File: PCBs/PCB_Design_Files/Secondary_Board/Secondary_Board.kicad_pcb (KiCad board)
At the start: 2 copper layers, 0 parts

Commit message: Bandgap/Ptat layout on secondary board. Updated grounded mounting holes on schematic, fix all DRC warnings
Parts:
- added C1: .1u, Project Footprints:0603_capacitor, F.Cu at (132.1, 94.5)
- added H1: MountingHole_Pad, MountingHole:MountingHole_2.2mm_M2_DIN965_Pad, F.Cu at (144.7, 70.4)
- added H2: MountingHole_Pad, MountingHole:MountingHole_2.2mm_M2_DIN965_Pad, F.Cu at (111.4, 70.4)
- added H3: MountingHole_Pad, MountingHole:MountingHole_2.2mm_M2_DIN965_Pad, F.Cu at (145.0, 120.0)
- added H4: MountingHole_Pad, MountingHole:MountingHole_2.2mm_M2_DIN965_Pad, F.Cu at (111.0, 120.0)
- added IC1: TLV2333IDGKR, Project Footprints:TLV2333IDGKR, F.Cu at (127.8, 94.7)
- added Q1: DMMT3904W-7-F, Project Footprints:DMMT3904W_Dual_NPN, F.Cu at (127.7, 88.8)
- added Q2: DMMT3904W-7-F, Project Footprints:DMMT3904W_Dual_NPN, F.Cu at (127.7, 85.8)
- added R3: 40k, Project Footprints:0603_resistor, F.Cu at (135.1, 94.4)
- added R4: 2.5k, Project Footprints:0603_resistor, F.Cu at (119.0, 87.2)
- added R5: 5k, Project Footprints:0603_resistor, F.Cu at (119.0, 91.0)
- added R6: 1k, Project Footprints:0603_resistor, F.Cu at (119.0, 83.4)
- added R7: 1k, Project Footprints:0603_resistor, F.Cu at (122.4, 82.5)
- added R8: 103, Project Footprints:0603_resistor, F.Cu at (132.6, 85.9)
- added R9: 2040, Project Footprints:0603_resistor, F.Cu at (127.5, 91.6)
- added U1: DMMT5401-7-F, Project Footprints:DMMT5401_Dual_PNP, F.Cu at (133.8, 90.3)
- added U2: DMMT5401-7-F, Project Footprints:DMMT5401_Dual_PNP, F.Cu at (121.7, 94.7)
- added U3: DMMT5401-7-F, Project Footprints:DMMT5401_Dual_PNP, F.Cu at (122.7, 90.0)
- added U4: DMMT5401-7-F, Project Footprints:DMMT5401_Dual_PNP, F.Cu at (122.6, 85.9)
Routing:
- net Net-(IC1-OUT_B): track 0.00 -> 32.6 mm, vias 0 -> 2
- net Net-(IC1-+IN_B): track 0.00 -> 31.5 mm
- net Net-(IC1--IN_A): track 0.00 -> 21.7 mm
- net Net-(IC1-+IN_A): track 0.00 -> 13.6 mm, vias 0 -> 2
- net GND: track 0.00 -> 13.1 mm, vias 0 -> 7
- net Net-(IC1-OUT_A): track 0.00 -> 11.4 mm
- net Net-(Q1-B2): track 0.00 -> 11.0 mm
- net /PTAT_Bandgap/V_bandgap: track 0.00 -> 10.7 mm
- net +3V3: track 0.00 -> 6.36 mm, vias 0 -> 5
- net Net-(U1-B1): track 0.00 -> 5.67 mm
- net Net-(U4-E1): track 0.00 -> 5.26 mm
- net Net-(U4-E2): track 0.00 -> 4.80 mm
- net /PTAT_Bandgap/V_ptat: track 0.00 -> 2.78 mm
- added copper zone on In2.Cu, net (none)
- added copper zone on F.Cu, net +3V3
- added copper zone on In2.Cu, net +3V3
- added copper zone on In1.Cu, net GND
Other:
- board outline added: 40.3 x 57.1 mm
- copper layers 2 -> 4
- rule pad_to_mask_clearance: 1 -> 0
- board text added: "CONTACT BELOW"

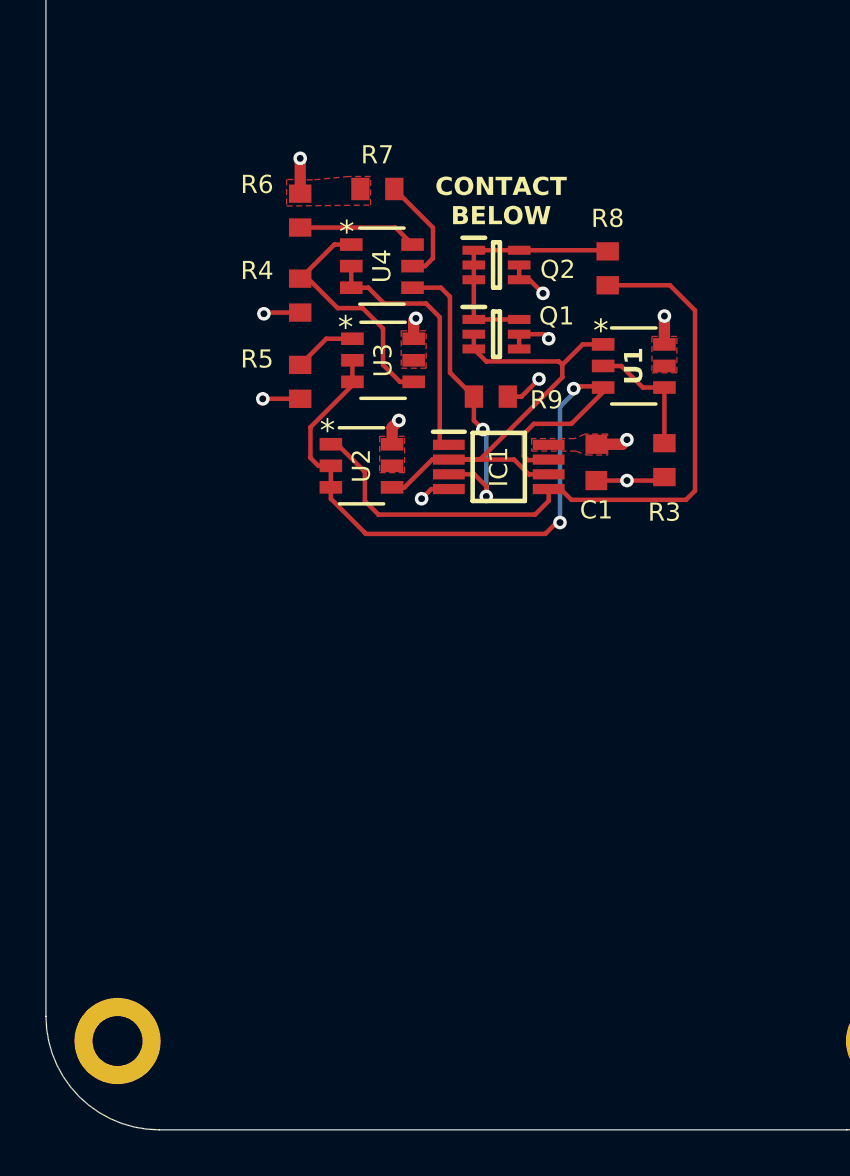
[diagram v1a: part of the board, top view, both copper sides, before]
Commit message: Added header and ffc connector to both boards + update libraries. Updated BOM
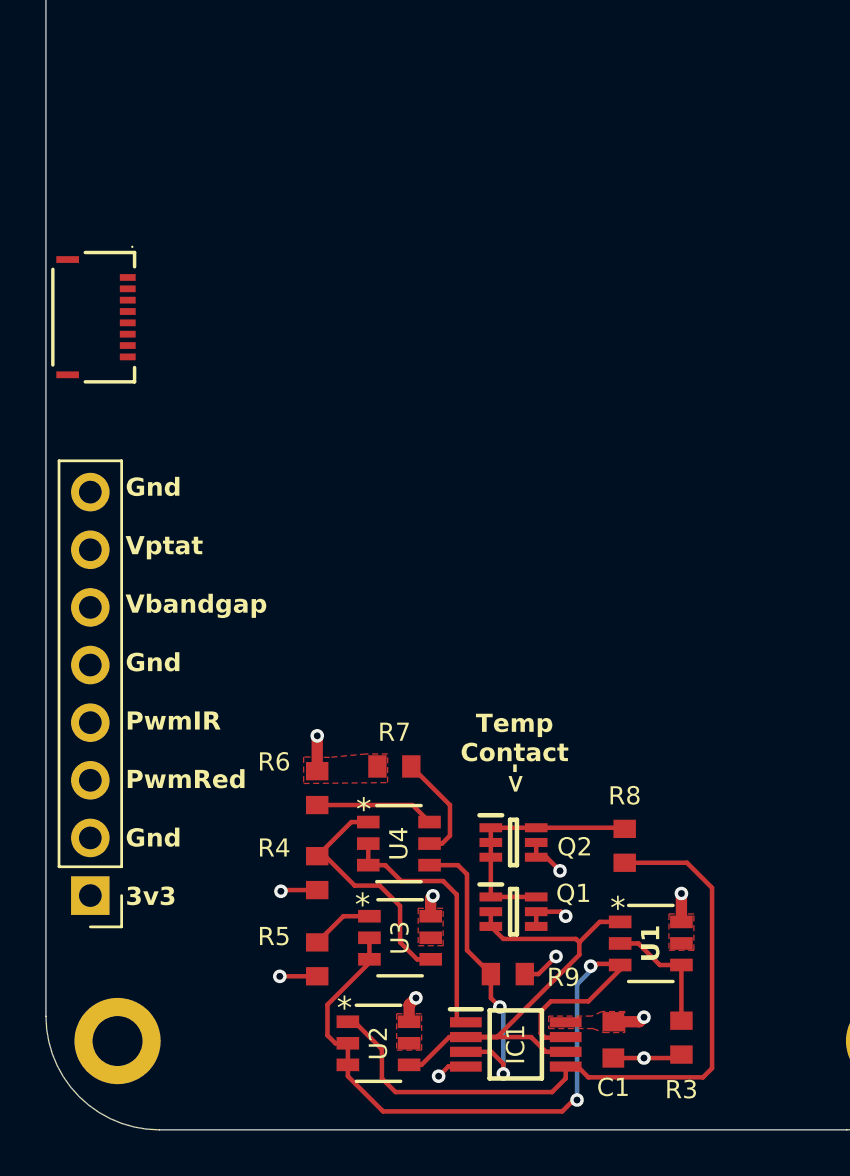
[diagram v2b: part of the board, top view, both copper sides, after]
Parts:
- added J1: Conn_FFC_8pin, Project Footprints:Conn_FFC_8pin, F.Cu at (110.0, 88.1)
- added J2: Conn_01x08_Pin, Connector_PinHeader_2.54mm:PinHeader_1x08_P2.54mm_Vertical, F.Cu at (109.8, 113.6)
- moved C1 25.5 mm to (132.8, 120.0)
- moved IC1 25.5 mm to (128.6, 120.2)
- moved R4 25.5 mm to (119.8, 112.6)
- moved R5 25.5 mm to (119.8, 116.4)
- moved R7 25.5 mm to (123.2, 107.9)
- moved R8 25.5 mm to (133.3, 111.4)
- moved U1 25.5 mm to (134.5, 115.7)
- moved U2 25.5 mm to (122.5, 120.1)
- moved U3 25.5 mm to (123.5, 115.5)
- moved Q1 25.5 mm to (128.4, 114.3)
- moved Q2 25.5 mm to (128.4, 111.2)
- moved R9 25.5 mm to (128.2, 117.0)
- moved R3 25.5 mm to (135.8, 119.8)
- moved R6 25.5 mm to (119.8, 108.9)
- moved U4 25.5 mm to (123.4, 111.3)
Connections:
- net /PTAT_Bandgap/V_bandgap renamed /V_bandgap
- net /PTAT_Bandgap/V_ptat renamed /V_ptat
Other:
- board text added: "->"
- board text added: "Gnd Vptat Vbandgap Gnd PwmIR PwmRed Gnd 3v3"
- board text added: "Temp Contact"
- board text removed: "CONTACT BELOW"

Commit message: update
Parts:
- added BT1: Battery, Connector_JST:JST_PH_S2B-PH-K_1x02_P2.00mm_Horizontal, F.Cu at (120.5, 86.0)
- added C2: 4.7u, Capacitor_SMD:C_0603_1608Metric, F.Cu at (120.5, 80.0)
- added C3: 4.7u, Capacitor_SMD:C_0603_1608Metric, F.Cu at (120.5, 81.5)
- added C4: 4.7u, Capacitor_SMD:C_0603_1608Metric, F.Cu at (86.0, 71.5)
- added C5: 4.7u, Capacitor_SMD:C_0603_1608Metric, F.Cu at (86.0, 74.0)
- added C6: 4.7u, Capacitor_SMD:C_0603_1608Metric, F.Cu at (86.0, 76.5)
- added C7: 4.7u, Capacitor_SMD:C_0603_1608Metric, F.Cu at (86.0, 79.0)
- added D1: 15N122B, Diode_THT:D_DO-35_SOD27_P7.62mm_Horizontal, F.Cu at (89.6, 67.0)
- added L1: CIGT201610LH1R0MNE, Project Footprints:RES_CIGT201610_SAM, F.Cu at (90.3, 80.2)
- added Q3: MMBT3904, Project Footprints:SOT23_FAS, F.Cu at (91.5, 71.2)
- added Q4: MMBT3904, Project Footprints:SOT23_FAS, F.Cu at (91.5, 76.1)
- added R1: 73.2k, Project Footprints:0603_resistor, F.Cu at (81.7, 66.8)
- added R10: 250, Project Footprints:0603_resistor, F.Cu at (81.7, 73.1)
- added R11: 100, Project Footprints:0603_resistor, F.Cu at (81.7, 76.3)
- added R12: 3.96k, Project Footprints:0603_resistor, F.Cu at (81.7, 79.4)
- added R13: 10k, Project Footprints:0603_resistor, F.Cu at (81.7, 82.6)
- added R2: 10k, Project Footprints:0603_resistor, F.Cu at (81.7, 69.9)
- added U5: TPS61023DRLR, Project Footprints:DRL0006A, F.Cu at (123.5, 79.5)
- added U6: TLV9101IDCKR, Project Footprints:SC70-5_DCK_TEX, F.Cu at (96.1, 80.6)
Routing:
- net +3.7V: track 0.00 -> 1.72 mm
- net Net-(U5-SW): track 0.00 -> 1.62 mm

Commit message: updated bg_ptat
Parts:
- added C8: .1u, Project Footprints:0603_capacitor, F.Cu at (116.2, 111.4)
- added U7: TLV9002, Project Footprints:TLV9002, F.Cu at (116.5, 114.6)
- R4: value 2.5k -> 2.2k
- R8: value 103 -> 105
- R9: value 2040 -> 2050
- moved C1 1.41 mm to (134.2, 120.1)
- moved Q1 1.41 mm to (129.8, 114.5)
- moved Q2 1.41 mm to (129.8, 111.4)
- moved R3 1.41 mm to (137.2, 120.0)
- moved R8 1.41 mm to (134.7, 111.5)
- moved R9 1.41 mm to (129.6, 117.2)
- moved U1 1.41 mm to (135.9, 115.9)
- moved U4 1.41 mm to (124.8, 111.5)
- moved R5 1.41 mm to (121.2, 116.6)
- moved R6 1.41 mm to (121.2, 109.0)
- moved R7 1.41 mm to (124.6, 108.1)
- moved U3 1.41 mm to (124.8, 115.6)
- moved R4 1.41 mm to (121.2, 112.8)
- moved U2 1.41 mm to (123.9, 120.3)
- moved IC1 1.41 mm to (129.9, 120.3)
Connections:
- J1 pad 2: GND -> +5V
- J1 pad 6: /V_bandgap -> /V_ptat
- J1 pad 7: /V_ptat -> /V_bandgap
- J2 pad 2: GND -> +5V
- J2 pad 6: /V_bandgap -> /V_ptat
- J2 pad 7: /V_ptat -> /V_bandgap
- R4 pad 1: /V_bandgap -> /PTAT_Bandgap/Vbg
- R5 pad 1: /V_ptat -> /PTAT_Bandgap/Vptat
- U3 pad 1: /V_ptat -> /PTAT_Bandgap/Vptat
- U3 pad 4: /V_bandgap -> /PTAT_Bandgap/Vbg
- U4 pad 1: /V_bandgap -> /PTAT_Bandgap/Vbg
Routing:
- net /V_ptat: track 2.78 -> 19.2 mm
- net /PTAT_Bandgap/Vbg: track 0.00 -> 15.4 mm
- net /V_bandgap: track 10.7 -> 21.4 mm
- net /PTAT_Bandgap/Vptat: track 0.00 -> 8.37 mm
- net GND: track 13.1 -> 16.0 mm, vias 7 -> 9
- net +3V3: track 6.36 -> 8.06 mm, vias 5 -> 6
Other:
- board text added: "Gnd Vbandgap Vptat Gnd PwmIR PwmRed Gnd 3v3"
- board text removed: "Gnd Vptat Vbandgap Gnd PwmIR PwmRed Gnd 3v3"

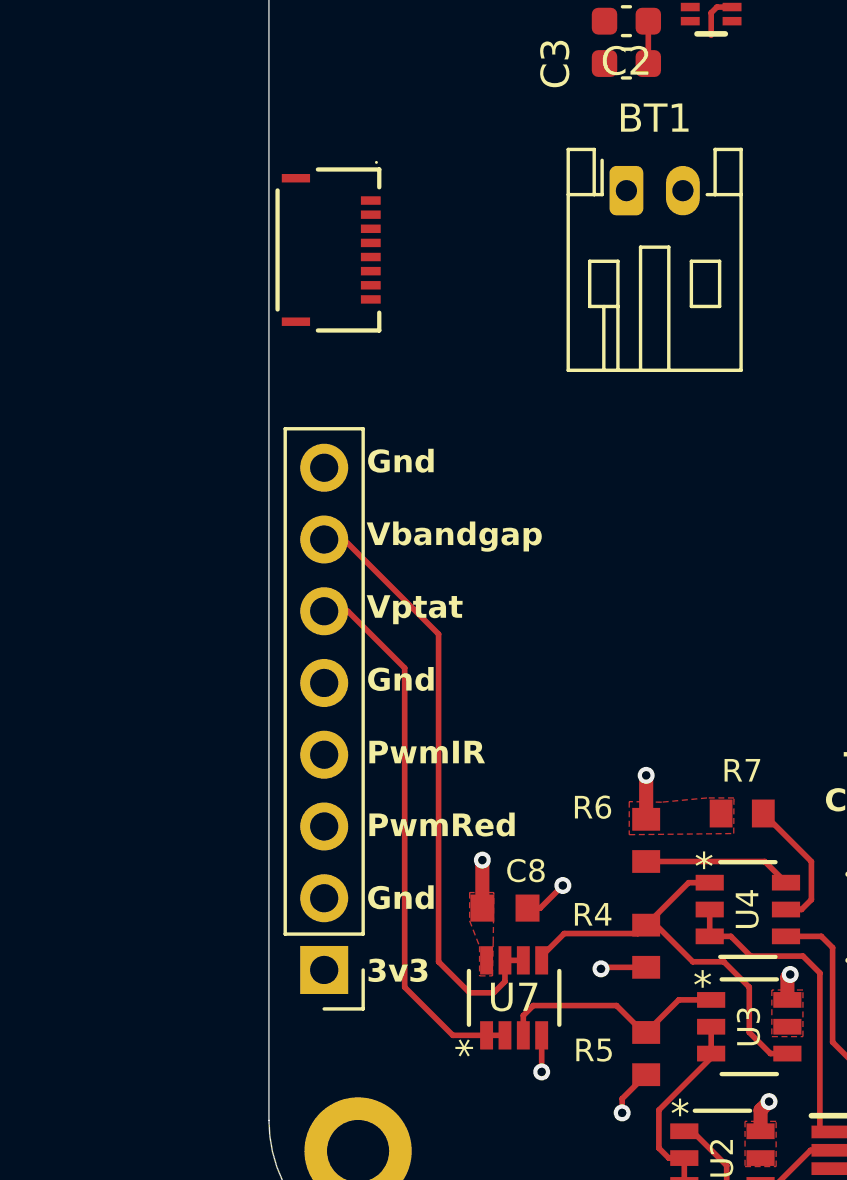
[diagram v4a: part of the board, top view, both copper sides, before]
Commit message: connected connectors
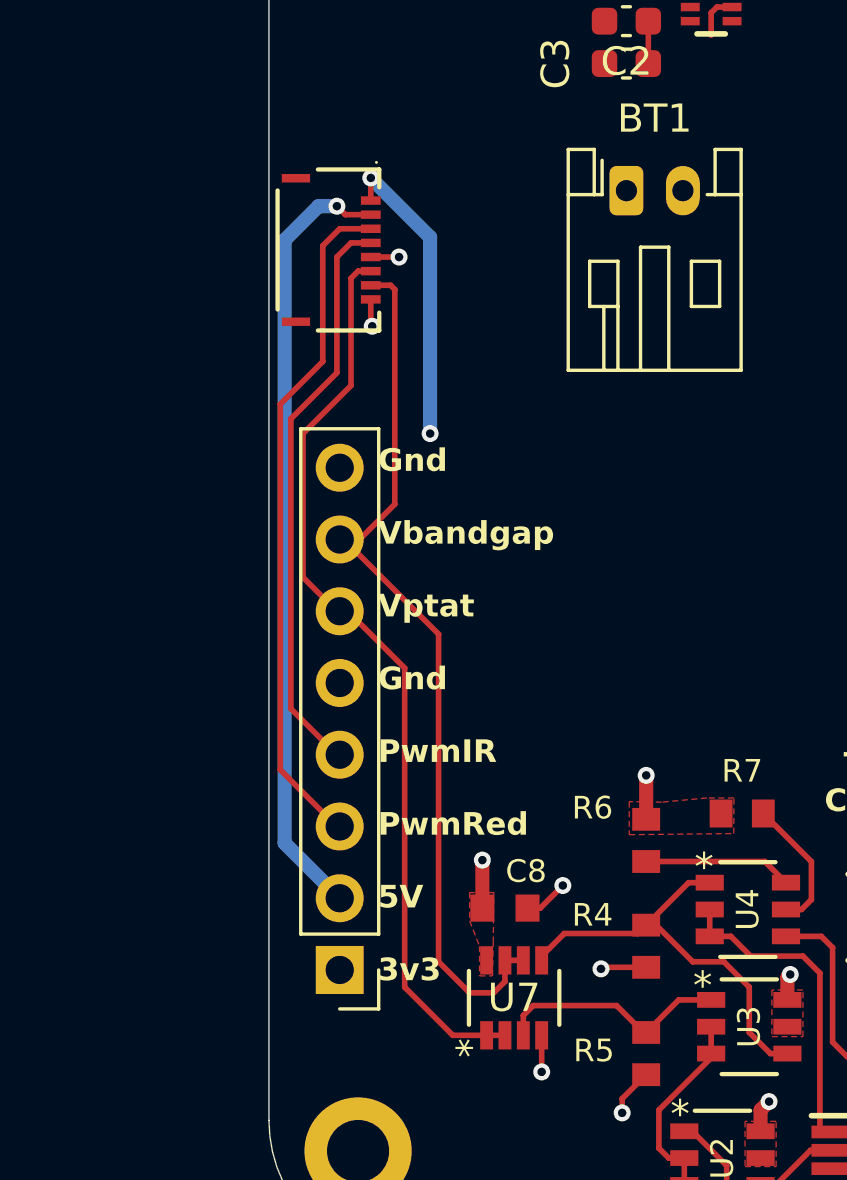
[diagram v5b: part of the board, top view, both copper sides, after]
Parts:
- moved J2 0.55 mm to (110.3, 113.6)
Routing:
- net +5V: track 0.00 -> 27.8 mm, vias 0 -> 1
- net /PWM_Red: track 0.00 -> 24.0 mm
- net /PWM_IR: track 0.00 -> 20.4 mm
- net /V_ptat: track 19.2 -> 33.0 mm
- net /V_bandgap: track 21.4 -> 32.5 mm
- net +3V3: track 8.06 -> 18.8 mm, vias 6 -> 8
- net GND: track 16.0 -> 18.0 mm, vias 9 -> 11
- added copper zone on In2.Cu, net +5V
- removed copper zone on In2.Cu, net (none)
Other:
- board text added: "Gnd Vbandgap Vptat Gnd PwmIR PwmRed 5V 3v3"
- board text removed: "Gnd Vbandgap Vptat Gnd PwmIR PwmRed Gnd 3v3"

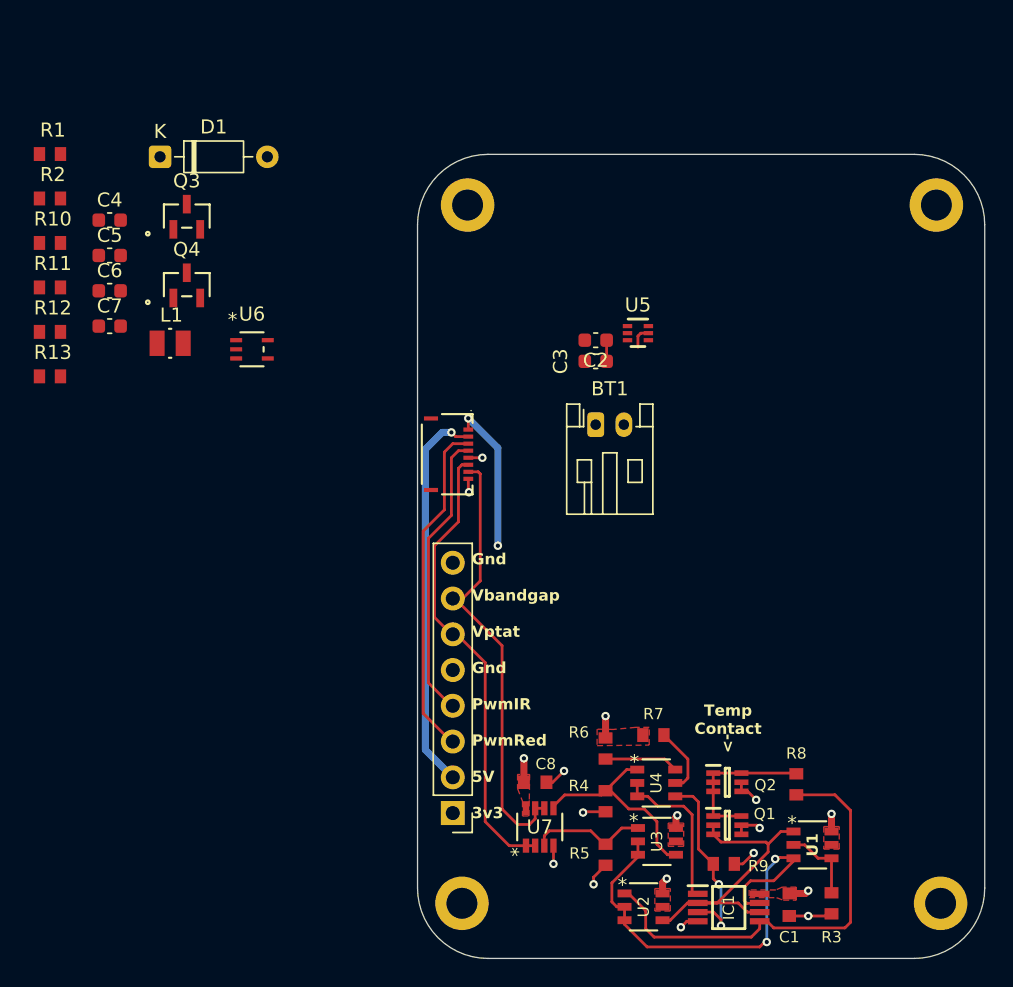
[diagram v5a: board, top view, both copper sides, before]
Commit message: boost to PCB
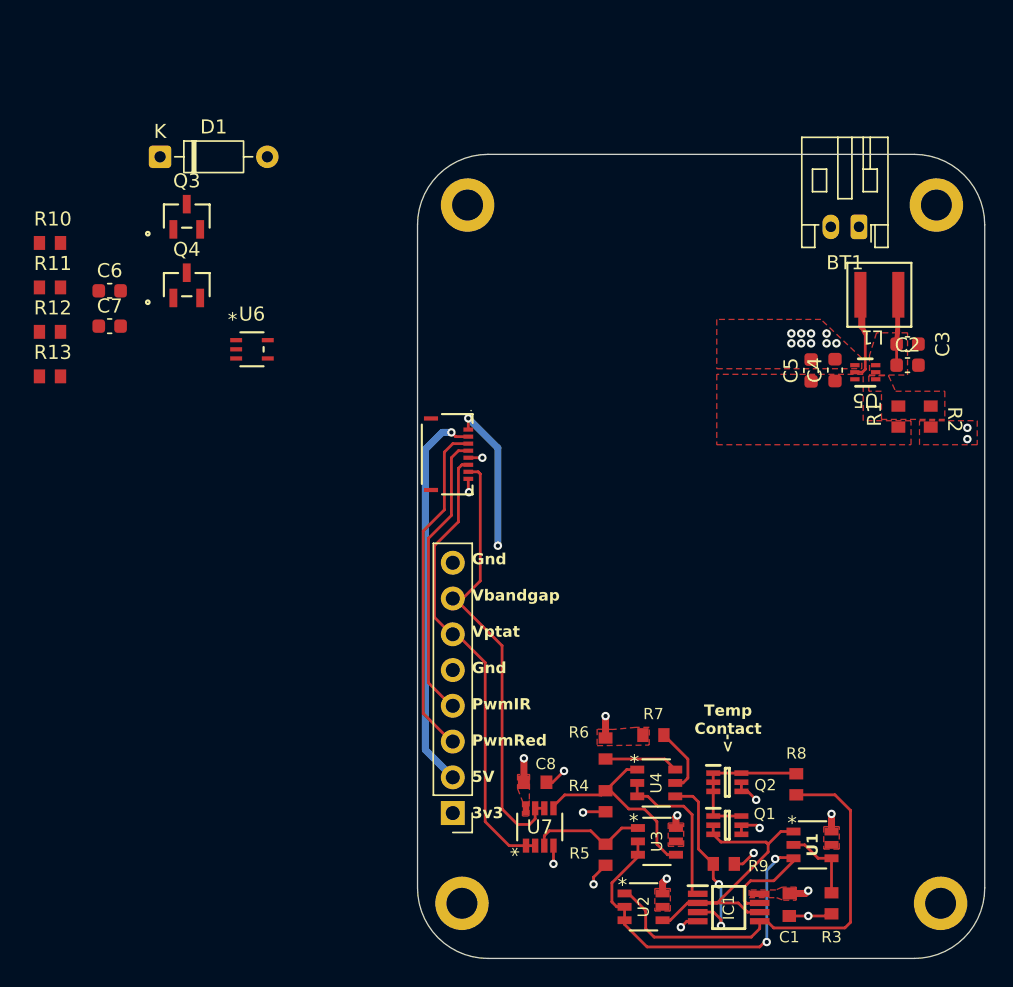
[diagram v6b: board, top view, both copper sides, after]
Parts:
- C4, C5: value 4.7u -> 22u
- L1: value CIGT201610LH1R0MNE -> XEL4030-102MEB; footprint Project Footprints:RES_CIGT201610_SAM -> Project Footprints:IND_XEL4030_3.1_COC
- R1: value 73.2k -> 732k
- R2: value 10k -> 100k
- moved R2 64.5 mm to (144.3, 85.4), turned to -90 degrees
- moved R1 63.1 mm to (142.0, 85.4), turned to 90 degrees
- moved C4 52.6 mm to (137.5, 82.1), turned to 90 degrees
- moved L1 50.5 mm to (140.7, 76.8), turned to 180 degrees
- moved C5 50.5 mm to (135.8, 82.2), turned to 90 degrees
- moved BT1 23.4 mm to (139.2, 72.0), turned to 180 degrees
- moved C2 22.2 mm to (142.7, 81.8), turned to 0 degrees
- moved C3 22.2 mm to (142.7, 80.3), turned to 0 degrees
- moved U5 16.4 mm to (139.7, 82.3), turned to 180 degrees
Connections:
- net Net-(U5-FB) renamed /Power Management/Vfb
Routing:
- net GND: vias 11 -> 22
- added copper zone on F.Cu, net +3.7V
- added copper zone on F.Cu, net /Power Management/+5V
- added copper zone on F.Cu, net /Power Management/Vfb
- added copper zone on F.Cu, net GND
